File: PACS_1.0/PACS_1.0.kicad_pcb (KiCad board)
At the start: 2 copper layers, 46 parts, among them J1 Conn_01x04_Socket, J2 Conn_01x02_Pin, Q1 PN2222A, U1 MSP430G2553IN20, U2 S-80855CNMC-B9GT2U, U3 BSS84PH6327XTSA2, U4 TPS562201DDCR, U5 MCP9700Ax-ETT, U6 LTR-303ALS-01

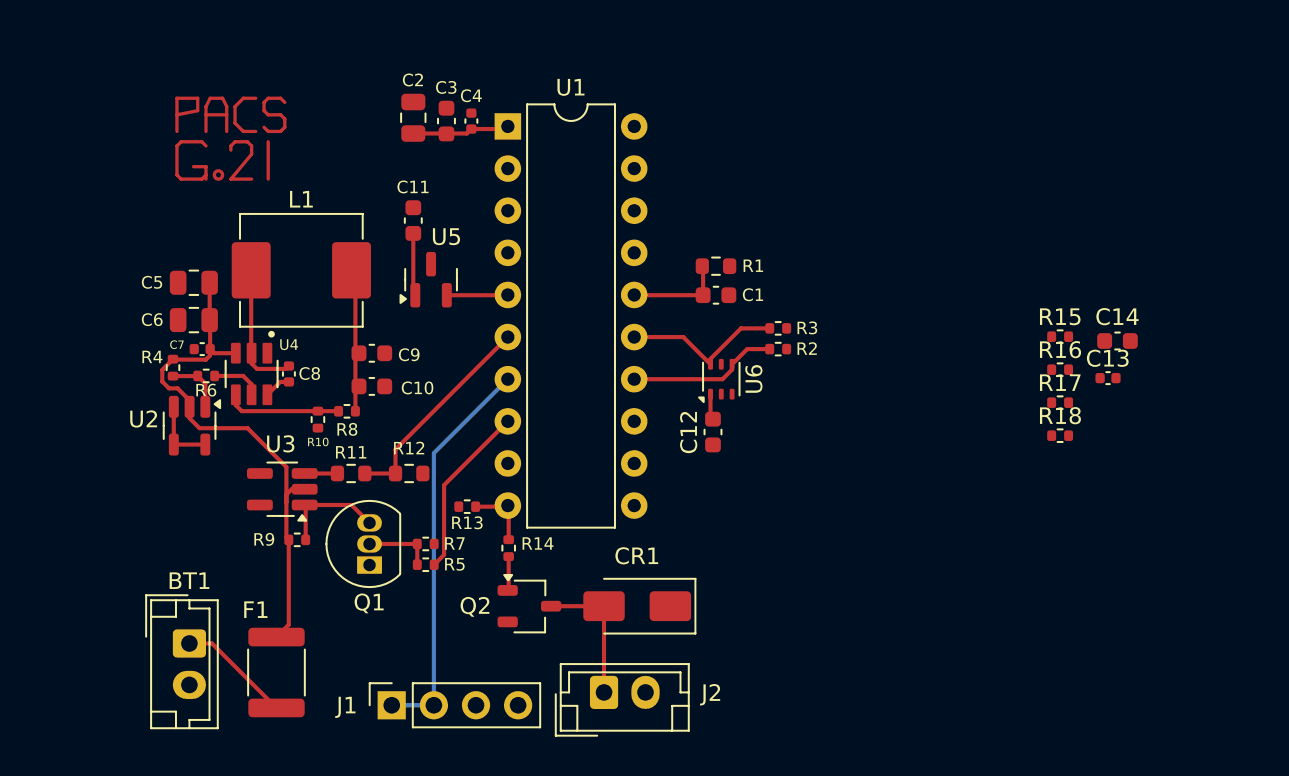
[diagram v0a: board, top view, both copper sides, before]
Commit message: FINISHED PCB DESIGN
must double check that the dimensions for XBee footprint are correct
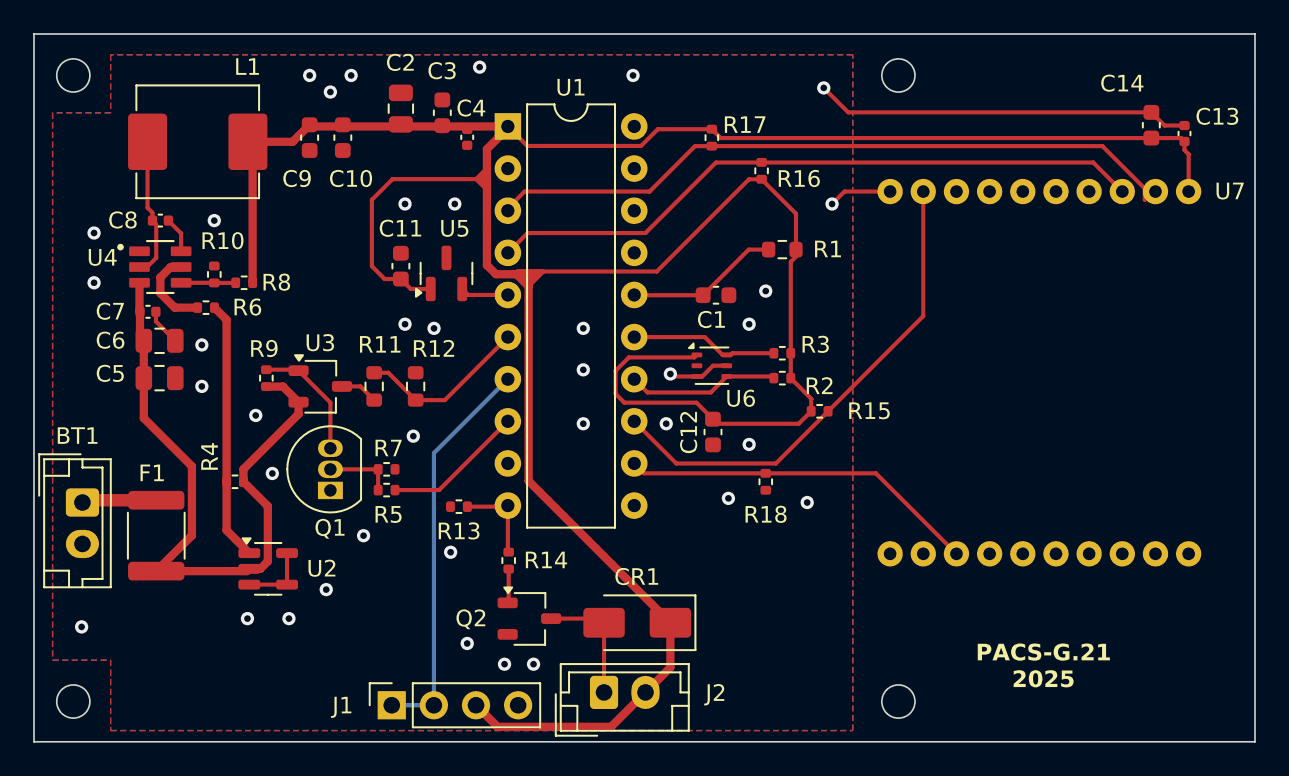
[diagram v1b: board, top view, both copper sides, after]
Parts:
- added U7: XB24CZ7WIT-004, RF_Module:XB24CZ7WIT-004, F.Cu at (203.7, 69.1)
- U3: footprint Package_TO_SOT_SMD:SOT-23-5_HandSoldering -> Package_TO_SOT_SMD:TSOT-23
- moved R17 26.4 mm to (184.0, 75.0), turned to -90 degrees
- moved R16 21.6 mm to (187.0, 77.0), turned to 90 degrees
- moved R18 18.0 mm to (187.2, 95.8), turned to -90 degrees
- moved C13 15.5 mm to (212.5, 74.8), turned to 90 degrees
- moved R15 15.2 mm to (190.5, 91.5)
- moved C10 15.1 mm to (161.8, 75.0), turned to -90 degrees
- moved C9 13.5 mm to (159.8, 75.0), turned to -90 degrees
- moved C14 13.2 mm to (210.5, 74.2), turned to 90 degrees
- moved C8 12.1 mm to (150.8, 80.0), turned to 180 degrees
- moved F1 11.0 mm to (150.5, 99.0), turned to -90 degrees
- moved R10 10.8 mm to (154.0, 83.2), turned to 90 degrees
- moved BT1 10.7 mm to (146.1, 97.0)
- moved L1 9.96 mm to (153.0, 75.2)
- moved R9 9.93 mm to (157.1, 89.5), turned to 90 degrees
- moved R8 9.92 mm to (155.8, 83.8)
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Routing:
- net +3.3V: track 20.0 -> 189.4 mm
- net /Zigbee Module/Tx: track 0.00 -> 42.6 mm
- net /Zigbee Module/Rx: track 0.00 -> 40.0 mm
- net GND: track 4.31 -> 36.6 mm, vias 0 -> 38
- net /Zigbee Module/SLEEP_RQ: track 0.00 -> 29.7 mm
- net /Zigbee Module/Sleep_Indicator: track 0.00 -> 21.7 mm
- net Net-(U2-OUT): track 3.55 -> 15.7 mm
- net Net-(U2-VDD): track 33.0 -> 40.5 mm
- net Net-(U4-VFB): track 6.97 -> 3.30 mm
- net Net-(U1-~{RST}/NMI/SBWTDIO): track 5.93 -> 9.25 mm
- net Net-(BT1-+): track 6.86 -> 4.26 mm
- net /Power/A_Voltage: track 12.9 -> 10.3 mm
- net Net-(U4-EN): track 3.07 -> 5.07 mm
- net /Power/VD_ON/OFF: track 10.5 -> 8.52 mm
- net /Actuators/PWM_Pump: track 4.04 -> 5.29 mm
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- added copper zone on B.Cu, net GND
- added copper zone on F.Cu, net GND
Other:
- board outline added: 73.6 x 42.7 mm
- board text added: "PACS-G.21 2025"

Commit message: added stitching vias, still need more
fix library issues
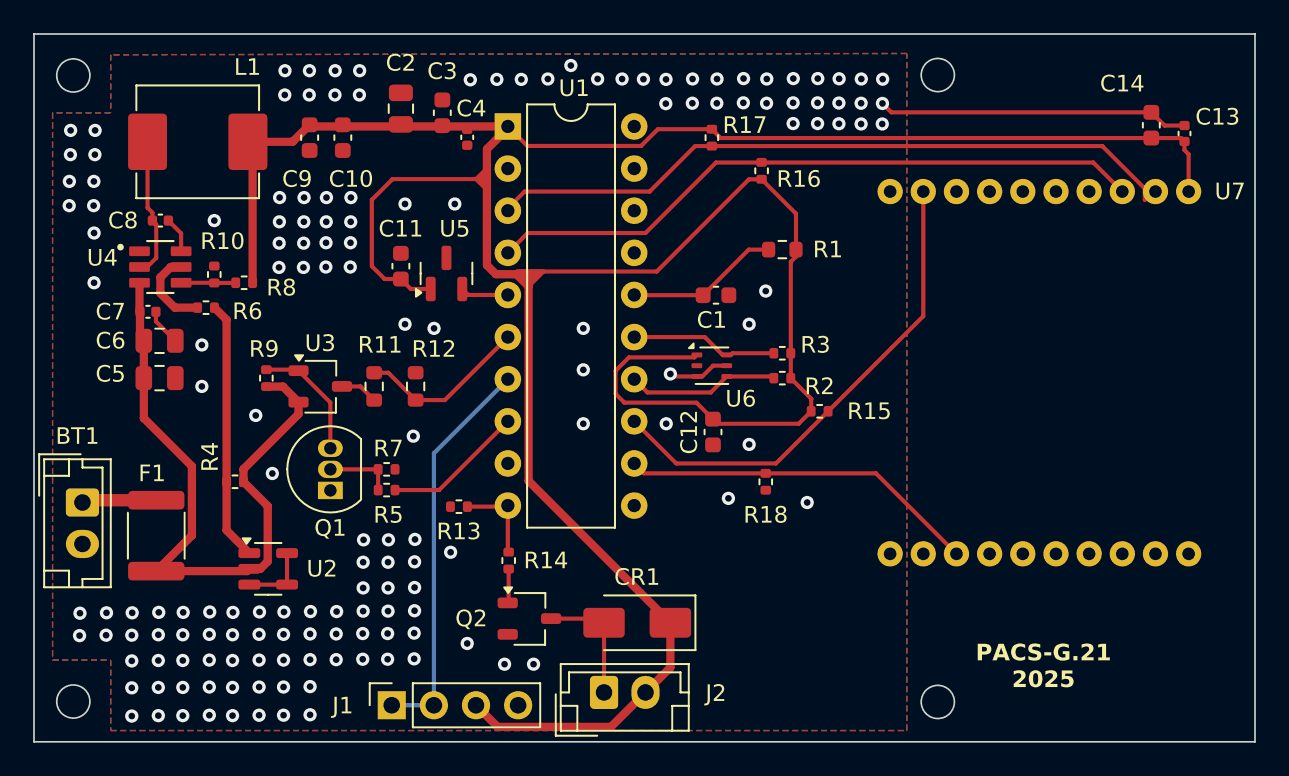
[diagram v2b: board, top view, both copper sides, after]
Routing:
- net GND: track 36.6 -> 28.9 mm, vias 38 -> 156
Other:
- outline, holes or cut-outs redrawn

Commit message: Added stitching vias
added names to backside of pcb
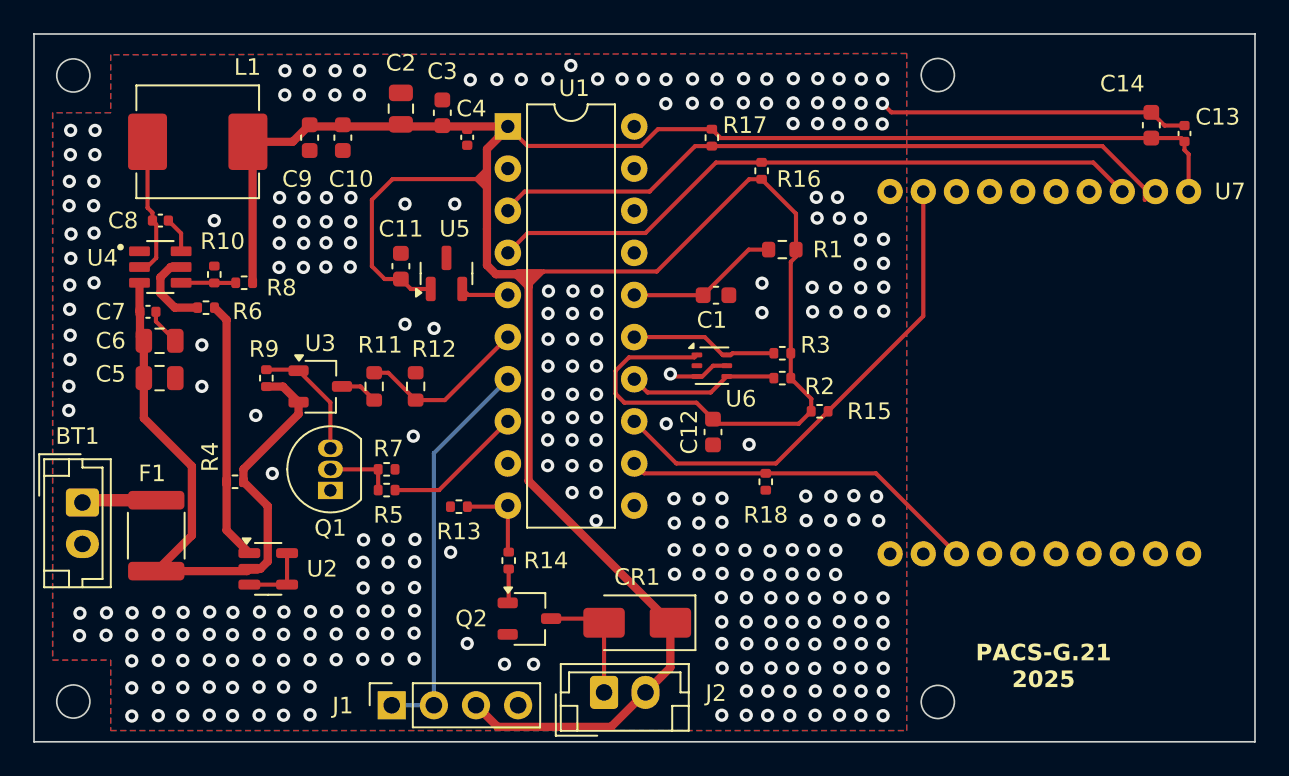
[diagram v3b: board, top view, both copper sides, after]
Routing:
- net GND: vias 156 -> 280
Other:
- board text added: "Jad Dib Melwin Moncy Noah Fares Jerushah Alexander"
